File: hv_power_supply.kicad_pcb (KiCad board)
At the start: 2 copper layers, 57.1 x 53.3 mm, 18 parts, among them P1 J1, P2 J2, P3 J3, P4 CONN_01X03, Q1 IRF644PBF, U1 MAX1771, U2 MCP41050

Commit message: Add holes and labels
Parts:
- added REF**: 1pin, Connect:1pin, F.Cu at (165.1, 90.2)
- added REF**: 1pin, Connect:1pin, F.Cu at (165.1, 138.4)
- added REF**: 1pin, Connect:1pin, F.Cu at (113.0, 138.4)
- added REF**: 1pin, Connect:1pin, F.Cu at (113.0, 90.2)
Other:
- outline, holes or cut-outs redrawn
- board text added: "CLK"
- board text added: "CS"
- board text added: "GND"
- board text added: "HV power supply v1.0 https://github.com/wheeler-microfluidics/ kicad___hv_power_supply"
- board text added: "HV+"
- board text added: "HV-"
- board text added: "PWR"
- board text added: "SI"
- board text added: "Shdn"
- board text added: "Vcc"
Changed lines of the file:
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@@
     (area 110.414999 87.554999 167.715001 141.045001)
     (thickness 1.6)
-    (drawings 8)
+    (drawings 14)
     (tracks 134)
     (zones 0)
-    (modules 18)
+    (modules 22)
     (nets 15)
   )
@@
     (mod_text_size 1 1)
     (mod_text_width 0.15)
-    (pad_size 5.99948 5.99948)
-    (pad_drill 1)
+    (pad_size 3.5 3.5)
+    (pad_drill 3.048)
     (pad_to_mask_clearance 0.2)
     (aux_axis_origin 0 0)
@@
     (add_net "Net-(R1-Pad1)")
     (add_net "Net-(R2-Pad2)")
+  )
+  (module Connect:1pin (layer F.Cu)
+    (at 165.1 90.17)
+    (descr "module 1 pin (ou trou mecanique de percage)")
+    (tags DEV)
+    (fp_text reference REF** (at 0 -1.27) (layer F.SilkS) hide
+      (effects (font (size 1 1) (thickness 0.15)))
+    )
+    (fp_text value 1pin (at 0 2.794) (layer F.Fab) hide
+      (effects (font (size 1 1) (thickness 0.15)))
+    )
+    (fp_circle (center 0 0) (end 0 2) (layer F.SilkS) (width 0.15))
+    (pad 1 thru_hole circle (at 0 0) (size 3.5 3.5) (drill 3.048) (layers *.Cu *.Mask F.SilkS))
+  )
+  (module Connect:1pin (layer F.Cu)
+    (at 165.1 138.43)
+    (descr "module 1 pin (ou trou mecanique de percage)")
+    (tags DEV)
+    (fp_text reference REF** (at 0 -3.048) (layer F.SilkS) hide
+      (effects (font (size 1 1) (thickness 0.15)))
+    )
+    (fp_text value 1pin (at 0 1.27) (layer F.Fab) hide
+      (effects (font (size 1 1) (thickness 0.15)))
+    )
+    (fp_circle (center 0 0) (end 0 2) (layer F.SilkS) (width 0.15))
+    (pad 1 thru_hole circle (at 0 0) (size 3.5 3.5) (drill 3.048) (layers *.Cu *.Mask F.SilkS))
+  )
+  (module Connect:1pin (layer F.Cu)
+    (at 113.03 138.43)
+    (descr "module 1 pin (ou trou mecanique de percage)")
+    (tags DEV)
+    (fp_text reference REF** (at 0 -3.048) (layer F.SilkS) hide
+      (effects (font (size 1 1) (thickness 0.15)))
+    )
+    (fp_text value 1pin (at 0 1.27) (layer F.Fab) hide
+      (effects (font (size 1 1) (thickness 0.15)))
+    )
+    (fp_circle (center 0 0) (end 0 2) (layer F.SilkS) (width 0.15))
+    (pad 1 thru_hole circle (at 0 0) (size 3.5 3.5) (drill 3.048) (layers *.Cu *.Mask F.SilkS))
+  )
+  (module Connect:1pin (layer F.Cu)
+    (at 113.03 90.17)
+    (descr "module 1 pin (ou trou mecanique de percage)")
+    (tags DEV)
+    (fp_text reference REF** (at 0 -1.27) (layer F.SilkS) hide
+      (effects (font (size 1 1) (thickness 0.15)))
+    )
+    (fp_text value 1pin (at 0 2.794) (layer F.Fab) hide
+      (effects (font (size 1 1) (thickness 0.15)))
+    )
+    (fp_circle (center 0 0) (end 0 2) (layer F.SilkS) (width 0.15))
+    (pad 1 thru_hole circle (at 0 0) (size 3.5 3.5) (drill 3.048) (layers *.Cu *.Mask F.SilkS))
   )
   (module Capacitors_SMD:c_elec_8x10.5 (layer F.Cu)
@@
       (effects (font (size 1 1) (thickness 0.15)))
     )
-    (fp_text value CONN_01X03 (at -2.54 2.54 180) (layer F.Fab) hide
+    (fp_text value CONN_01X03 (at 2.54 2.54 180) (layer F.Fab)
       (effects (font (size 1 1) (thickness 0.15)))
     )
@@
     )
   )
+  (gr_text "HV power supply v1.0\nhttps://github.com/wheeler-microfluidics/\n  kicad___hv_power_supply" (at 115.57 91.44) (layer F.SilkS)
+    (effects (font (size 1.2 1) (thickness 0.15)) (justify left))
+  )
+  (gr_text HV+ (at 162.56 135.89) (layer F.SilkS)
+    (effects (font (size 1 1.2) (thickness 0.15)))
+  )
+  (gr_text HV- (at 157.48 135.89) (layer F.SilkS)
+    (effects (font (size 1 1.2) (thickness 0.15)))
+  )
+  (gr_text SI (at 149.86 135.89) (layer F.SilkS)
+    (effects (font (size 1 1.2) (thickness 0.15)))
+  )
+  (gr_text CLK (at 146.05 135.89) (layer F.SilkS)
+    (effects (font (size 1 1.2) (thickness 0.15)))
+  )
+  (gr_text CS (at 142.24 135.89) (layer F.SilkS)
+    (effects (font (size 1 1.2) (thickness 0.15)))
+  )
+  (gr_text Shdn (at 133.35 135.89) (layer F.SilkS)
+    (effects (font (size 1 1.2) (thickness 0.15)))
+  )
+  (gr_text GND (at 128.27 135.89) (layer F.SilkS)
+    (effects (font (size 1 1.2) (thickness 0.15)))
+  )
+  (gr_text Vcc (at 120.65 135.89) (layer F.SilkS)
+    (effects (font (size 1 1.2) (thickness 0.15)))
+  )
+  (gr_text PWR (at 115.57 135.89) (layer F.SilkS)
+    (effects (font (size 1 1.2) (thickness 0.15)))
+  )
   (gr_line (start 110.49 140.97) (end 110.49 87.63) (angle 90) (layer Edge.Cuts) (width 0.15))
   (gr_line (start 167.64 140.97) (end 110.49 140.97) (angle 90) (layer Edge.Cuts) (width 0.15))
   (gr_line (start 167.64 87.63) (end 167.64 140.97) (angle 90) (layer Edge.Cuts) (width 0.15))
   (gr_line (start 110.49 87.63) (end 167.64 87.63) (angle 90) (layer Edge.Cuts) (width 0.15))
-  (gr_circle (center 165.1 138.43) (end 163.83 138.43) (layer Edge.Cuts) (width 0.15))
-  (gr_circle (center 113.03 138.43) (end 114.3 138.43) (layer Edge.Cuts) (width 0.15))
-  (gr_circle (center 113.03 90.17) (end 114.3 90.17) (layer Edge.Cuts) (width 0.15))
-  (gr_circle (center 165.1 90.17) (end 163.83 90.17) (layer Edge.Cuts) (width 0.15))
   (segment (start 150.368 116.078) (end 157.8483 116.078) (width 0.25) (layer B.Cu) (net 1))
   (segment (start 162.2425 113.03) (end 161.05 113.03) (width 0.25) (layer F.Cu) (net 1))
@@
     (polygon
       (pts
-        (xy 166.37 138.43) (xy 111.76 138.43) (xy 111.76 91.44) (xy 166.37 91.44) (xy 166.37 138.43)
+        (xy 166.37 139.7) (xy 111.76 139.7) (xy 111.76 88.9) (xy 166.37 88.9) (xy 166.37 138.43)
       )
     )

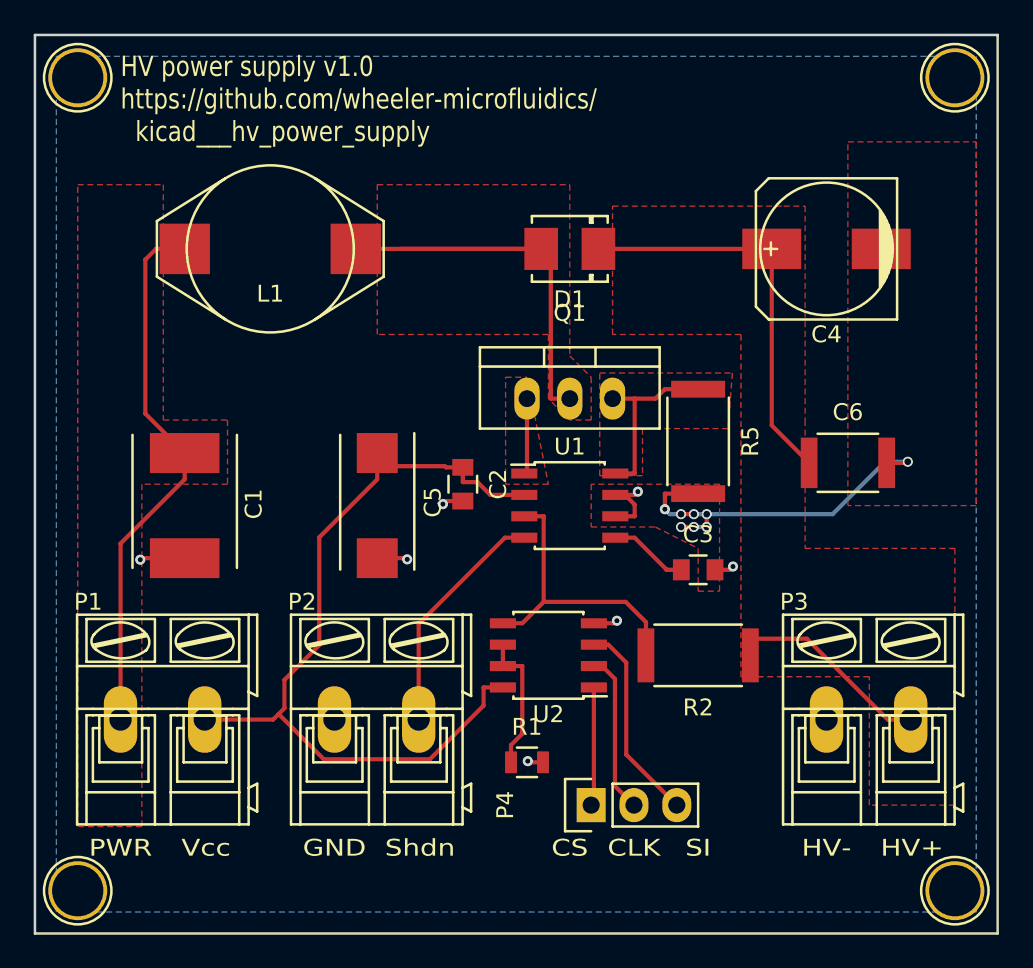
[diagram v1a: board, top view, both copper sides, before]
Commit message: Break out all pins on 9x1 header
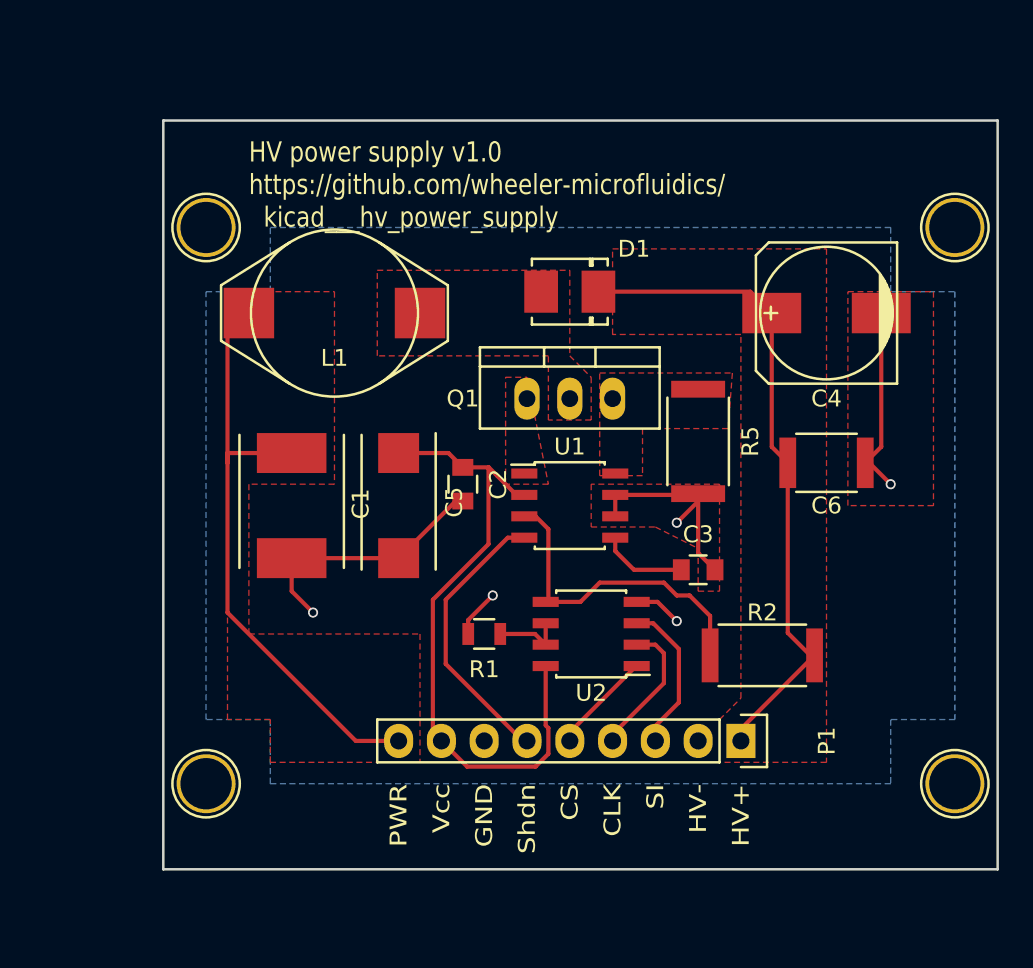
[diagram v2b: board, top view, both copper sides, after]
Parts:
- removed P2: J2, Connect:AK300-2
- removed P3: J3, Connect:AK300-2
- removed P4: CONN_01X03, Pin_Headers:Pin_Header_Straight_1x03
- P1: value J1 -> CONN_01X09; footprint Connect:AK300-2 -> Pin_Headers:Pin_Header_Straight_1x09
- moved P1 36.9 mm to (152.4, 129.5), turned to 270 degrees
- moved REF** 11.7 mm to (120.7, 99.1)
- moved REF** 9.92 mm to (120.7, 132.1)
- moved REF** 8.89 mm to (165.1, 99.1)
- moved R1 8.03 mm to (137.2, 123.2), turned to 180 degrees
- moved C1 6.35 mm to (125.7, 115.6)
- moved REF** 6.35 mm to (165.1, 132.1)
- moved L1 5.39 mm to (128.3, 104.1)
- moved C4 3.81 mm to (157.5, 104.1)
- moved R2 3.81 mm to (153.7, 124.5)
- moved U2 2.84 mm to (143.5, 123.2)
- moved D1 2.54 mm to (142.2, 102.9)
- moved C5 1.27 mm to (132.1, 115.6)
- moved C6 1.27 mm to (157.5, 113.0)
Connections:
- C1 pad 1: Net-(C1-Pad1) -> PWR
- C1 pad 2: GNDD -> DGND
- C2 pad 1: Net-(C2-Pad1) -> VCC
- C2 pad 2: GNDD -> DGND
- C3 pad 2: GNDD -> DGND
- C4 pad 1: Net-(C4-Pad1) -> HV
- C4 pad 2: GNDD -> DGND
- C5 pad 1: Net-(C2-Pad1) -> VCC
- C5 pad 2: GNDD -> DGND
- C6 pad 1: Net-(C4-Pad1) -> HV
- C6 pad 2: GNDD -> DGND
- D1 pad 1: Net-(C4-Pad1) -> HV
- L1 pad 2: Net-(C1-Pad1) -> PWR
- P1 pad 1: Net-(C1-Pad1) -> HV
- P1 pad 2: Net-(C2-Pad1) -> DGND
- R1 pad 2: GNDD -> DGND
- R2 pad 1: Net-(C4-Pad1) -> HV
- R5 pad 2: GNDD -> DGND
- U1 pad 2: Net-(C2-Pad1) -> VCC
- U1 pad 4: Net-(P2-Pad2) -> SHDN
- U1 pad 6: GNDD -> DGND
- U1 pad 7: GNDD -> DGND
- U2 pad 1: Net-(P4-Pad1) -> CS
- U2 pad 2: Net-(P4-Pad2) -> SCK
- U2 pad 3: Net-(P4-Pad3) -> SI
- U2 pad 4: GNDD -> DGND
- U2 pad 8: Net-(C2-Pad1) -> VCC
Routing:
- net Net-(C2-Pad1): track 49.2 -> 0.00 mm
- net DGND: track 0.00 -> 46.7 mm, vias 0 -> 5
- net HV: track 0.00 -> 39.0 mm
- net VCC: track 0.00 -> 38.9 mm
- net Net-(C4-Pad1): track 36.4 -> 0.00 mm
- net PWR: track 0.00 -> 36.0 mm
- net GNDD: track 35.9 -> 0.00 mm, vias 15 -> 0
- net Net-(C1-Pad1): track 32.5 -> 0.00 mm
- net Net-(D1-Pad2): track 29.5 -> 0.00 mm
- net SHDN: track 0.00 -> 16.9 mm
- net Net-(P2-Pad2): track 14.1 -> 0.00 mm
- net Net-(P4-Pad3): track 12.1 -> 0.00 mm
- net Net-(Q1-Pad3): track 10.9 -> 0.00 mm
- net Net-(P4-Pad2): track 10.1 -> 0.00 mm
- net SI: track 0.00 -> 9.18 mm
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- added copper zone on B.Cu, net DGND
- added copper zone on F.Cu, net DGND
- added copper zone on F.Cu, net HV
- added copper zone on F.Cu, net PWR
- removed copper zone on B.Cu, net GNDD
- removed copper zone on F.Cu, net GNDD
- removed copper zone on F.Cu, net Net-(C1-Pad1)
- removed copper zone on F.Cu, net Net-(C4-Pad1)
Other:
- board size 57.1 x 53.3 mm -> 49.5 x 44.5 mm
